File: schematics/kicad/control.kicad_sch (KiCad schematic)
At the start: 5 parts, among them U10 74F175, U42 PAL16L8, U43 PAL16L8, U44 PAL16L8, U45 PAL16L8

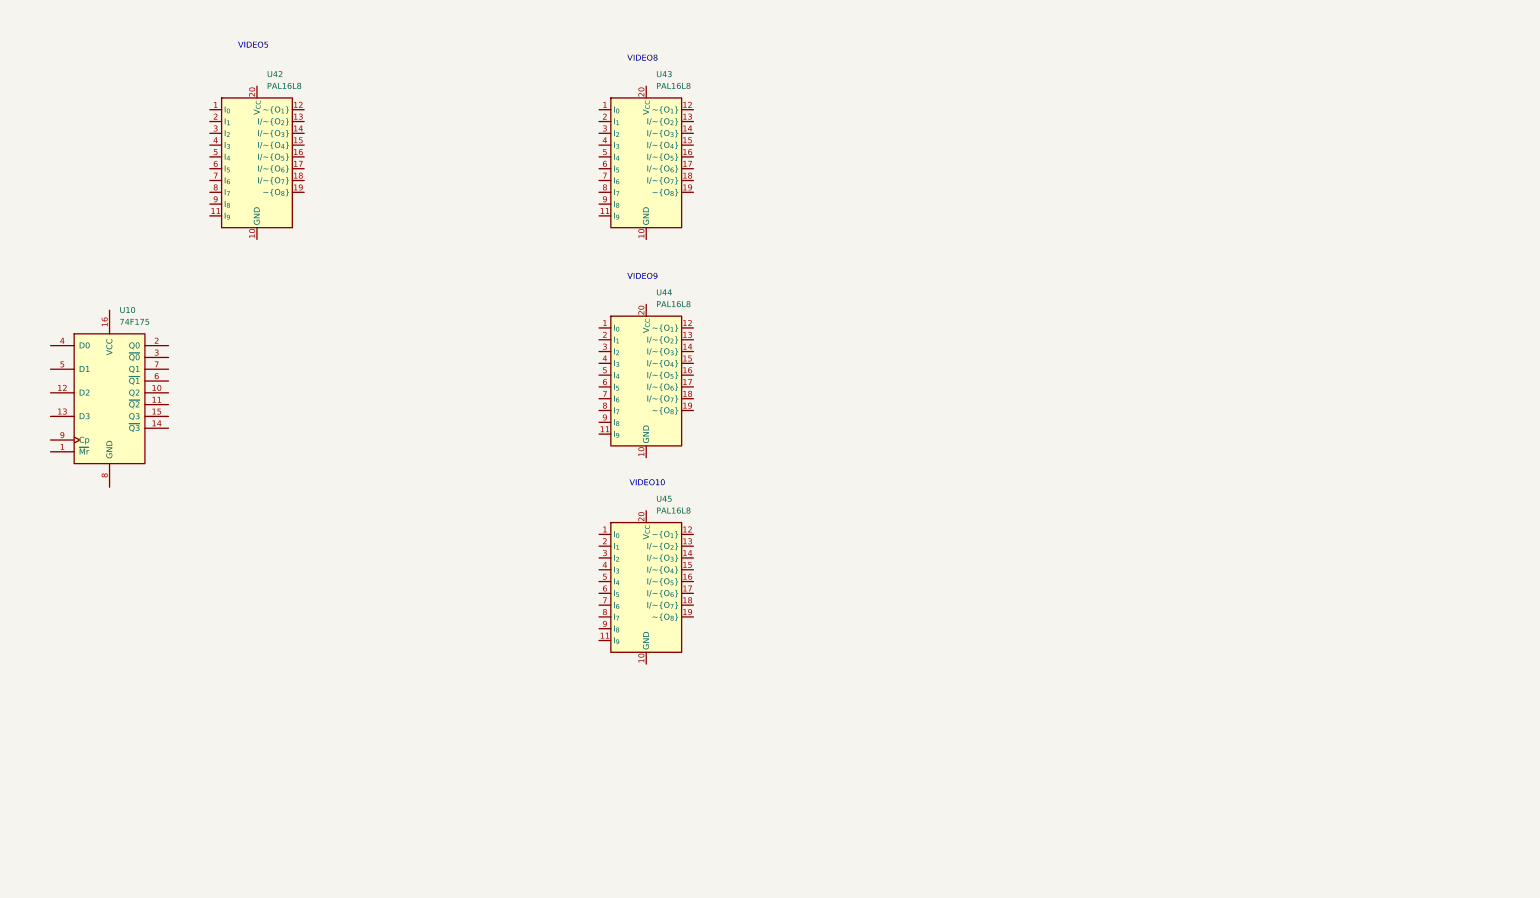
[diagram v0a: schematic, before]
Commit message: Populate misc page with P4 connector and caps Finish MUX, RAM and most of Output Lots of progress on Control Lay out root and connect most components
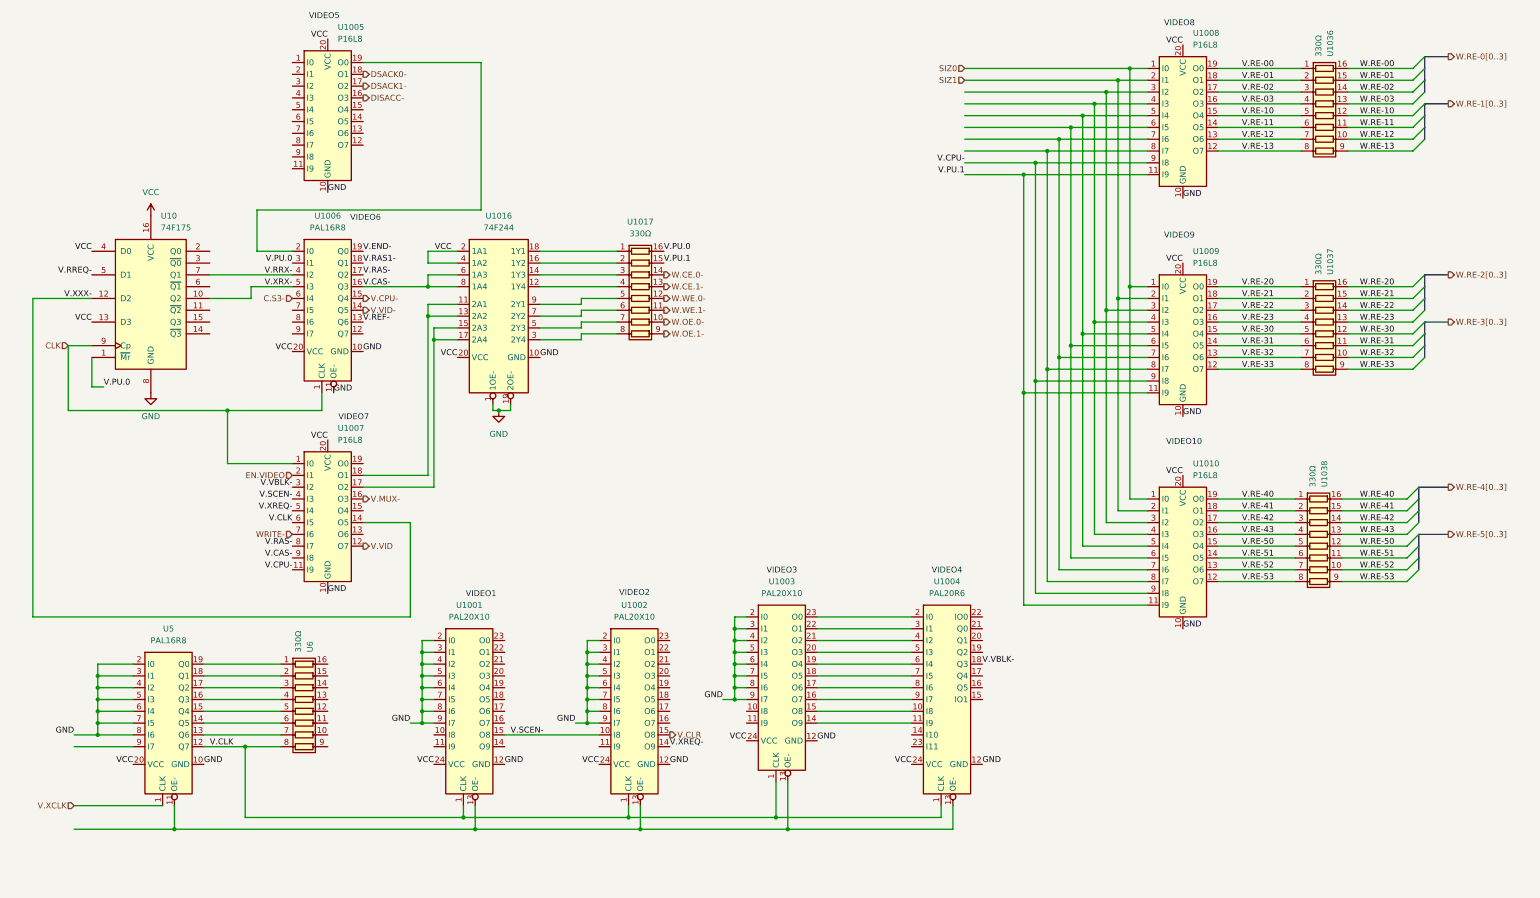
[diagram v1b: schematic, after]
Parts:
- removed U42, U43, U44, U45: PAL16L8, symbol Logic_Programmable:PAL16L8
- added U1001, U1002, U1003: PAL20X10, Package_DIP:DIP-24_W7.62mm, symbol cg4:P20X10
- added U1004: PAL20R6, Package_DIP:DIP-24_W7.62mm, symbol cg4:P20R6
- added U1005, U1007, U1008, U1009, U1010: P16L8, Package_DIP:DIP-20_W7.62mm, symbol cg4:P16L8
- added U1006, U5: PAL16R8, Package_DIP:DIP-20_W7.62mm, symbol cg4:P16R8
- added U1016: 74F244, Package_DIP:DIP-20_W7.62mm, symbol cg4:74F244
- added U1017, U1036, U1037, U1038, U6: 330Ω, Package_DIP:DIP-16_W7.62mm, symbol Device:R_Pack08
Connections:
- net V.PU.0: now reaches U10.1 (~{Mr})
- net V.PU.0: now also U1006.3 (I1), U1017.16 (R1.2)
- net V.XRX-: now reaches U10.10 (Q2)
- net V.XRX-: now also U1006.5 (I3)
- net V.XXX-: now reaches U10.12 (D2)
- net V.XXX-: now also U1007.14 (O5)
- net VCC: now reaches U10.13 (D3)
- net VCC: now also U10.16 (VCC), U10.4 (D0), U1001.24 (VCC), U1002.24 (VCC), U1003.24 (VCC), U1004.24 (VCC), U1005.20 (VCC), U1006.20 (VCC), U1007.20 (VCC), U1008.20 (VCC), U1009.20 (VCC), U1010.20 (VCC), U1016.2 (1A1), U1016.20 (VCC), U1016.4 (1A2), U5.20 (VCC)
- net V.RREQ-: now reaches U10.5 (D1)
- net V.RRX-: now reaches U10.7 (Q1)
- net V.RRX-: now also U1006.4 (I2)
- net GND: now reaches U10.8 (GND)
- net GND: now also U1001.12 (GND), U1001.2 (I0), U1001.3 (I1), U1001.4 (I2), U1001.5 (I3), U1001.6 (I4), U1001.7 (I5), U1001.8 (I6), U1001.9 (I7), U1002.12 (GND), U1002.2 (I0), U1002.3 (I1), U1002.4 (I2), U1002.5 (I3), U1002.6 (I4), U1002.7 (I5), U1002.8 (I6), U1002.9 (I7), U1003.12 (GND), U1003.2 (I0), U1003.3 (I1), U1003.4 (I2), U1003.5 (I3), U1003.6 (I4), U1003.7 (I5), U1003.8 (I6), U1003.9 (I7), U1004.12 (GND), U1005.10 (GND), U1006.10 (GND), U1006.11 (OE-), U1007.10 (GND), U1008.10 (GND), U1009.10 (GND), U1010.10 (GND), U1016.1 (1OE-), U1016.10 (GND), U1016.19 (2OE-), U5.10 (GND), U5.2 (I0), U5.3 (I1), U5.4 (I2), U5.5 (I3), U5.6 (I4), U5.7 (I5), U5.8 (I6)
- net CLK: now reaches U10.9 (Cp)
- net CLK: now also U1006.1 (CLK), U1007.1 (I0)
- new net: U1001.13 (OE-), U1002.13 (OE-), U1003.13 (OE-), U1004.13 (OE-), U5.11 (OE-)
- new net: U1003.14 (O9), U1004.11 (I9)
- new net: U1003.15 (O8), U1004.10 (I8)
- new net: U1003.16 (O7), U1004.9 (I7)
- new net: U1003.17 (O6), U1004.8 (I6)
- new net: U1003.18 (O5), U1004.7 (I5)
- new net: U1003.19 (O4), U1004.6 (I4)
- new net: U1003.20 (O3), U1004.5 (I3)
- new net: U1003.21 (O2), U1004.4 (I2)
- new net: U1003.22 (O1), U1004.3 (I1)
- new net: U1003.23 (O0), U1004.2 (I0)
- new net: U1008.3 (I2), U1009.3 (I2), U1010.3 (I2)
- new net: U1008.4 (I3), U1009.4 (I3), U1010.4 (I3)
- new net: U1008.5 (I4), U1009.5 (I4), U1010.5 (I4)
- new net: U1008.6 (I5), U1009.6 (I5), U1010.6 (I5)
- new net: U1008.7 (I6), U1009.7 (I6), U1010.7 (I6)
- new net: U1008.8 (I7), U1009.8 (I7), U1010.8 (I7)
- new net: U1005.19 (O0), U1006.2 (I0)
- new net: U1016.18 (1Y1), U1017.1 (R1.1)
- new net: U1016.16 (1Y2), U1017.2 (R2.1)
- new net: U1016.14 (1Y3), U1017.3 (R3.1)
- new net: U1016.12 (1Y4), U1017.4 (R4.1)
- new net: U1016.9 (2Y1), U1017.5 (R5.1)
- new net: U1016.7 (2Y2), U1017.6 (R6.1)
- new net: U1016.5 (2Y3), U1017.7 (R7.1)
- new net: U1016.3 (2Y4), U1017.8 (R8.1)
- new net: U1007.17 (O2), U1016.15 (2A3), U1016.17 (2A4)
- new net: U1007.18 (O1), U1016.11 (2A1), U1016.13 (2A2)
- new net: U5.13 (Q6), U6.7 (R7.1)
- new net: U5.14 (Q5), U6.6 (R6.1)
- new net: U5.15 (Q4), U6.5 (R5.1)
- new net: U5.16 (Q3), U6.4 (R4.1)
- new net: U5.17 (Q2), U6.3 (R3.1)
- new net: U5.18 (Q1), U6.2 (R2.1)
- new net: U5.19 (Q0), U6.1 (R1.1)
- new net C.S3-: U1006.6 (I4)
- new net DISACC-: U1005.16 (O3)
- new net DSACK0-: U1005.18 (O1)
- new net DSACK1-: U1005.17 (O2)
- new net EN.VIDEO: U1007.2 (I1)
- new net SIZ0: U1008.1 (I0), U1009.1 (I0), U1010.1 (I0)
- new net SIZ1: U1008.2 (I1), U1009.2 (I1), U1010.2 (I1)
- new net V.CAS-: U1006.16 (Q3), U1007.9 (I8), U1016.6 (1A3), U1016.8 (1A4)
- new net V.CLK: U1001.1 (CLK), U1002.1 (CLK), U1003.1 (CLK), U1004.1 (CLK), U1007.6 (I5), U5.12 (Q7), U6.8 (R8.1)
- new net V.CLR: U1002.15 (O8)
- new net V.CPU-: U1006.15 (Q4), U1007.11 (I9), U1008.9 (I8), U1009.9 (I8), U1010.9 (I8)
- new net V.END-: U1006.19 (Q0)
- new net V.MUX-: U1007.16 (O3)
- new net V.PU.1: U1008.11 (I9), U1009.11 (I9), U1010.11 (I9), U1017.15 (R2.2)
- new net V.RAS-: U1006.17 (Q2), U1007.8 (I7)
- new net V.RAS1-: U1006.18 (Q1)
- new net V.RE-00: U1008.19 (O0), U1036.1 (R1.1)
- new net V.RE-01: U1008.18 (O1), U1036.2 (R2.1)
- new net V.RE-02: U1008.17 (O2), U1036.3 (R3.1)
- new net V.RE-03: U1008.16 (O3), U1036.4 (R4.1)
- new net V.RE-10: U1008.15 (O4), U1036.5 (R5.1)
- new net V.RE-11: U1008.14 (O5), U1036.6 (R6.1)
- new net V.RE-12: U1008.13 (O6), U1036.7 (R7.1)
- new net V.RE-13: U1008.12 (O7), U1036.8 (R8.1)
- new net V.RE-20: U1009.19 (O0), U1037.1 (R1.1)
- new net V.RE-21: U1009.18 (O1), U1037.2 (R2.1)
- new net V.RE-22: U1009.17 (O2), U1037.3 (R3.1)
- new net V.RE-23: U1009.16 (O3), U1037.4 (R4.1)
- new net V.RE-30: U1009.15 (O4), U1037.5 (R5.1)
- new net V.RE-31: U1009.14 (O5), U1037.6 (R6.1)
- new net V.RE-32: U1009.13 (O6), U1037.7 (R7.1)
- new net V.RE-33: U1009.12 (O7), U1037.8 (R8.1)
- new net V.RE-40: U1010.19 (O0), U1038.1 (R1.1)
- new net V.RE-41: U1010.18 (O1), U1038.2 (R2.1)
- new net V.RE-42: U1010.17 (O2), U1038.3 (R3.1)
- new net V.RE-43: U1010.16 (O3), U1038.4 (R4.1)
- new net V.RE-50: U1010.15 (O4), U1038.5 (R5.1)
- new net V.RE-51: U1010.14 (O5), U1038.6 (R6.1)
- new net V.RE-52: U1010.13 (O6), U1038.7 (R7.1)
- new net V.RE-53: U1010.12 (O7), U1038.8 (R8.1)
- new net V.REF-: U1006.13 (Q6)
- new net V.SCEN-: U1001.15 (O8), U1002.10 (I8), U1007.4 (I3)
- new net V.VBLK-: U1004.18 (Q3), U1007.3 (I2)
- new net V.VID: U1007.12 (O7)
- new net V.VID-: U1006.14 (Q5)
- new net V.XCLK: U5.1 (CLK)
- new net V.XREQ-: U1002.14 (O9), U1007.5 (I4)
- new net W.CE.0-: U1017.14 (R3.2)
- new net W.CE.1-: U1017.13 (R4.2)
- new net W.OE.0-: U1017.10 (R7.2)
- new net W.OE.1-: U1017.9 (R8.2)
- new net W.RE-00: U1036.16 (R1.2)
- new net W.RE-01: U1036.15 (R2.2)
- new net W.RE-02: U1036.14 (R3.2)
- new net W.RE-03: U1036.13 (R4.2)
- new net W.RE-10: U1036.12 (R5.2)
- new net W.RE-11: U1036.11 (R6.2)
- new net W.RE-12: U1036.10 (R7.2)
- new net W.RE-13: U1036.9 (R8.2)
- new net W.RE-20: U1037.16 (R1.2)
- new net W.RE-21: U1037.15 (R2.2)
- new net W.RE-22: U1037.14 (R3.2)
- new net W.RE-23: U1037.13 (R4.2)
- new net W.RE-30: U1037.12 (R5.2)
- new net W.RE-31: U1037.11 (R6.2)
- new net W.RE-32: U1037.10 (R7.2)
- new net W.RE-33: U1037.9 (R8.2)
- new net W.RE-40: U1038.16 (R1.2)
- new net W.RE-41: U1038.15 (R2.2)
- new net W.RE-42: U1038.14 (R3.2)
- new net W.RE-43: U1038.13 (R4.2)
- new net W.RE-50: U1038.12 (R5.2)
- new net W.RE-51: U1038.11 (R6.2)
- new net W.RE-52: U1038.10 (R7.2)
- new net W.RE-53: U1038.9 (R8.2)
- new net W.WE.0-: U1017.12 (R5.2)
- new net W.WE.1-: U1017.11 (R6.2)
- new net WRITE-: U1007.7 (I6)
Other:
- note added: "VIDEO1"
- note added: "VIDEO2"
- note added: "VIDEO3"
- note added: "VIDEO4"
- note added: "VIDEO6"
- note added: "VIDEO7"
- moved on the sheet: U10

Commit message: Fill in most of control, wire up addresses, and more
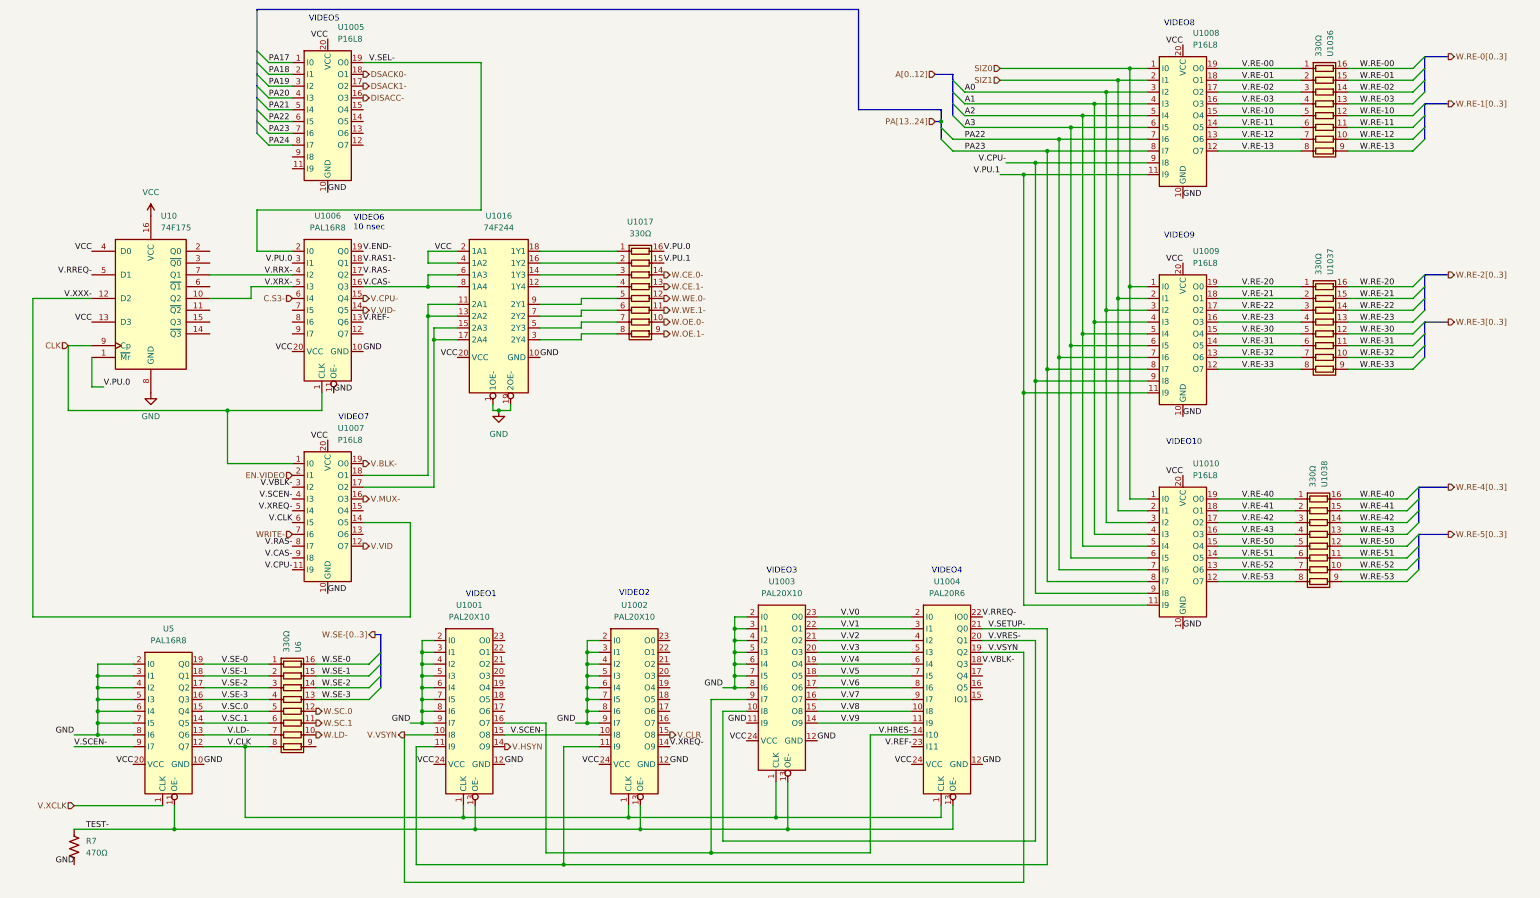
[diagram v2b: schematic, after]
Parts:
- added R7: 470Ω, symbol Device:R_US
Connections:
- net GND: now also U1003.11 (I9), R7.2; no longer U1003.9 (I7)
- net V.REF-: now also U1004.23 (I11)
- net V.RREQ-: now also U1004.22 (IO0)
- net V.SCEN-: now also U5.9 (I7)
- net V.VRES-: now reaches U1003.10 (I8)
- net V.VRES-: now also U1004.20 (Q1)
- net TEST-: now reaches U1001.13 (OE-), U1002.13 (OE-), U1003.13 (OE-), U1004.13 (OE-), U5.11 (OE-)
- net TEST-: now also R7.1
- net V.V9: now reaches U1003.14 (O9), U1004.11 (I9)
- net V.V8: now reaches U1003.15 (O8), U1004.10 (I8)
- net V.V7: now reaches U1003.16 (O7), U1004.9 (I7)
- net V.V6: now reaches U1003.17 (O6), U1004.8 (I6)
- net V.V5: now reaches U1003.18 (O5), U1004.7 (I5)
- net V.V4: now reaches U1003.19 (O4), U1004.6 (I4)
- net V.V3: now reaches U1003.20 (O3), U1004.5 (I3)
- net V.V2: now reaches U1003.21 (O2), U1004.4 (I2)
- net V.V1: now reaches U1003.22 (O1), U1004.3 (I1)
- net V.V0: now reaches U1003.23 (O0), U1004.2 (I0)
- net A0: now reaches U1008.3 (I2), U1009.3 (I2), U1010.3 (I2)
- net A1: now reaches U1008.4 (I3), U1009.4 (I3), U1010.4 (I3)
- net A2: now reaches U1008.5 (I4), U1009.5 (I4), U1010.5 (I4)
- net A3: now reaches U1008.6 (I5), U1009.6 (I5), U1010.6 (I5)
- net PA22: now reaches U1008.7 (I6), U1009.7 (I6), U1010.7 (I6)
- net PA22: now also U1005.6 (I5)
- net PA23: now reaches U1008.8 (I7), U1009.8 (I7), U1010.8 (I7)
- net PA23: now also U1005.7 (I6)
- net V.SETUP-: now reaches U1002.11 (I9)
- net V.SETUP-: now also U1001.11 (I9), U1004.21 (Q0)
- net PA17: now reaches U1005.1 (I0)
- net V.SEL-: now reaches U1005.19 (O0), U1006.2 (I0)
- net PA18: now reaches U1005.2 (I1)
- net PA19: now reaches U1005.3 (I2)
- net PA20: now reaches U1005.4 (I3)
- net PA21: now reaches U1005.5 (I4)
- net PA24: now reaches U1005.8 (I7)
- net V.HRES-: now reaches U1004.14 (I10)
- net V.HRES-: now also U1001.16 (O7), U1003.9 (I7)
- net V.VSYN: now reaches U1004.19 (Q2)
- net V.VSYN: now also U1001.10 (I8)
- net V.HSYN: now reaches U1001.14 (O9)
- net V.BLK-: now reaches U1007.19 (O0)
- net V.LD-: now reaches U5.13 (Q6), U6.7 (R7.1)
- net V.SC.1: now reaches U5.14 (Q5), U6.6 (R6.1)
- net V.SC.0: now reaches U5.15 (Q4), U6.5 (R5.1)
- net V.SE-3: now reaches U5.16 (Q3), U6.4 (R4.1)
- net V.SE-2: now reaches U5.17 (Q2), U6.3 (R3.1)
- net V.SE-1: now reaches U5.18 (Q1), U6.2 (R2.1)
- net V.SE-0: now reaches U5.19 (Q0), U6.1 (R1.1)
- net W.LD-: now reaches U6.10 (R7.2)
- net W.SC.1: now reaches U6.11 (R6.2)
- net W.SC.0: now reaches U6.12 (R5.2)
- net W.SE-3: now reaches U6.13 (R4.2)
- net W.SE-2: now reaches U6.14 (R3.2)
- net W.SE-1: now reaches U6.15 (R2.2)
- net W.SE-0: now reaches U6.16 (R1.2)
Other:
- note added: "VIDEO6 10 nsec"
- note removed: "VIDEO6"
- moved on the sheet: U6

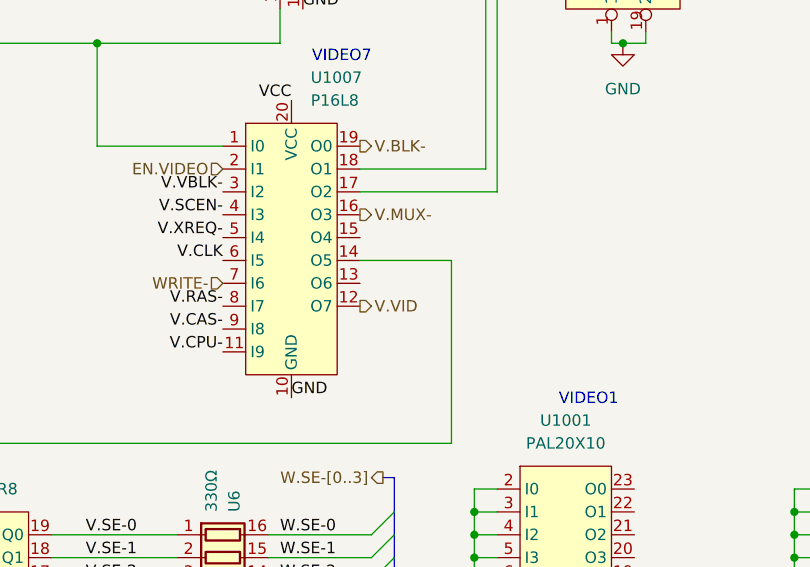
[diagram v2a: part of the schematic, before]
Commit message: Add datasheets
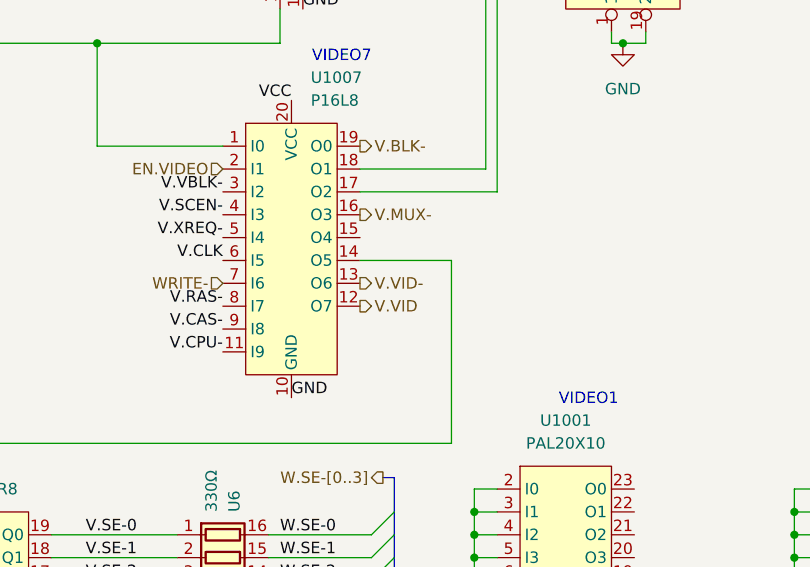
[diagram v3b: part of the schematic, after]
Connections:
- net V.VID-: now also U1007.13 (O6)
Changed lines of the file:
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@@
+		)
+	)
+	(hierarchical_label "V.VID-"
+		(shape output)
+		(at 92.71 125.73 0)
+		(effects
+			(font
+				(size 1.27 1.27)
+			)
+			(justify left)
 		)
 	)
